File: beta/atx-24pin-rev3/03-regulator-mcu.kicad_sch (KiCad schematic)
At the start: 18 parts, among them SW1 BOOT, SW2 RESET, U1 ESP32-C6-MINI-1-N4, U3 LP5907MFX-3.3

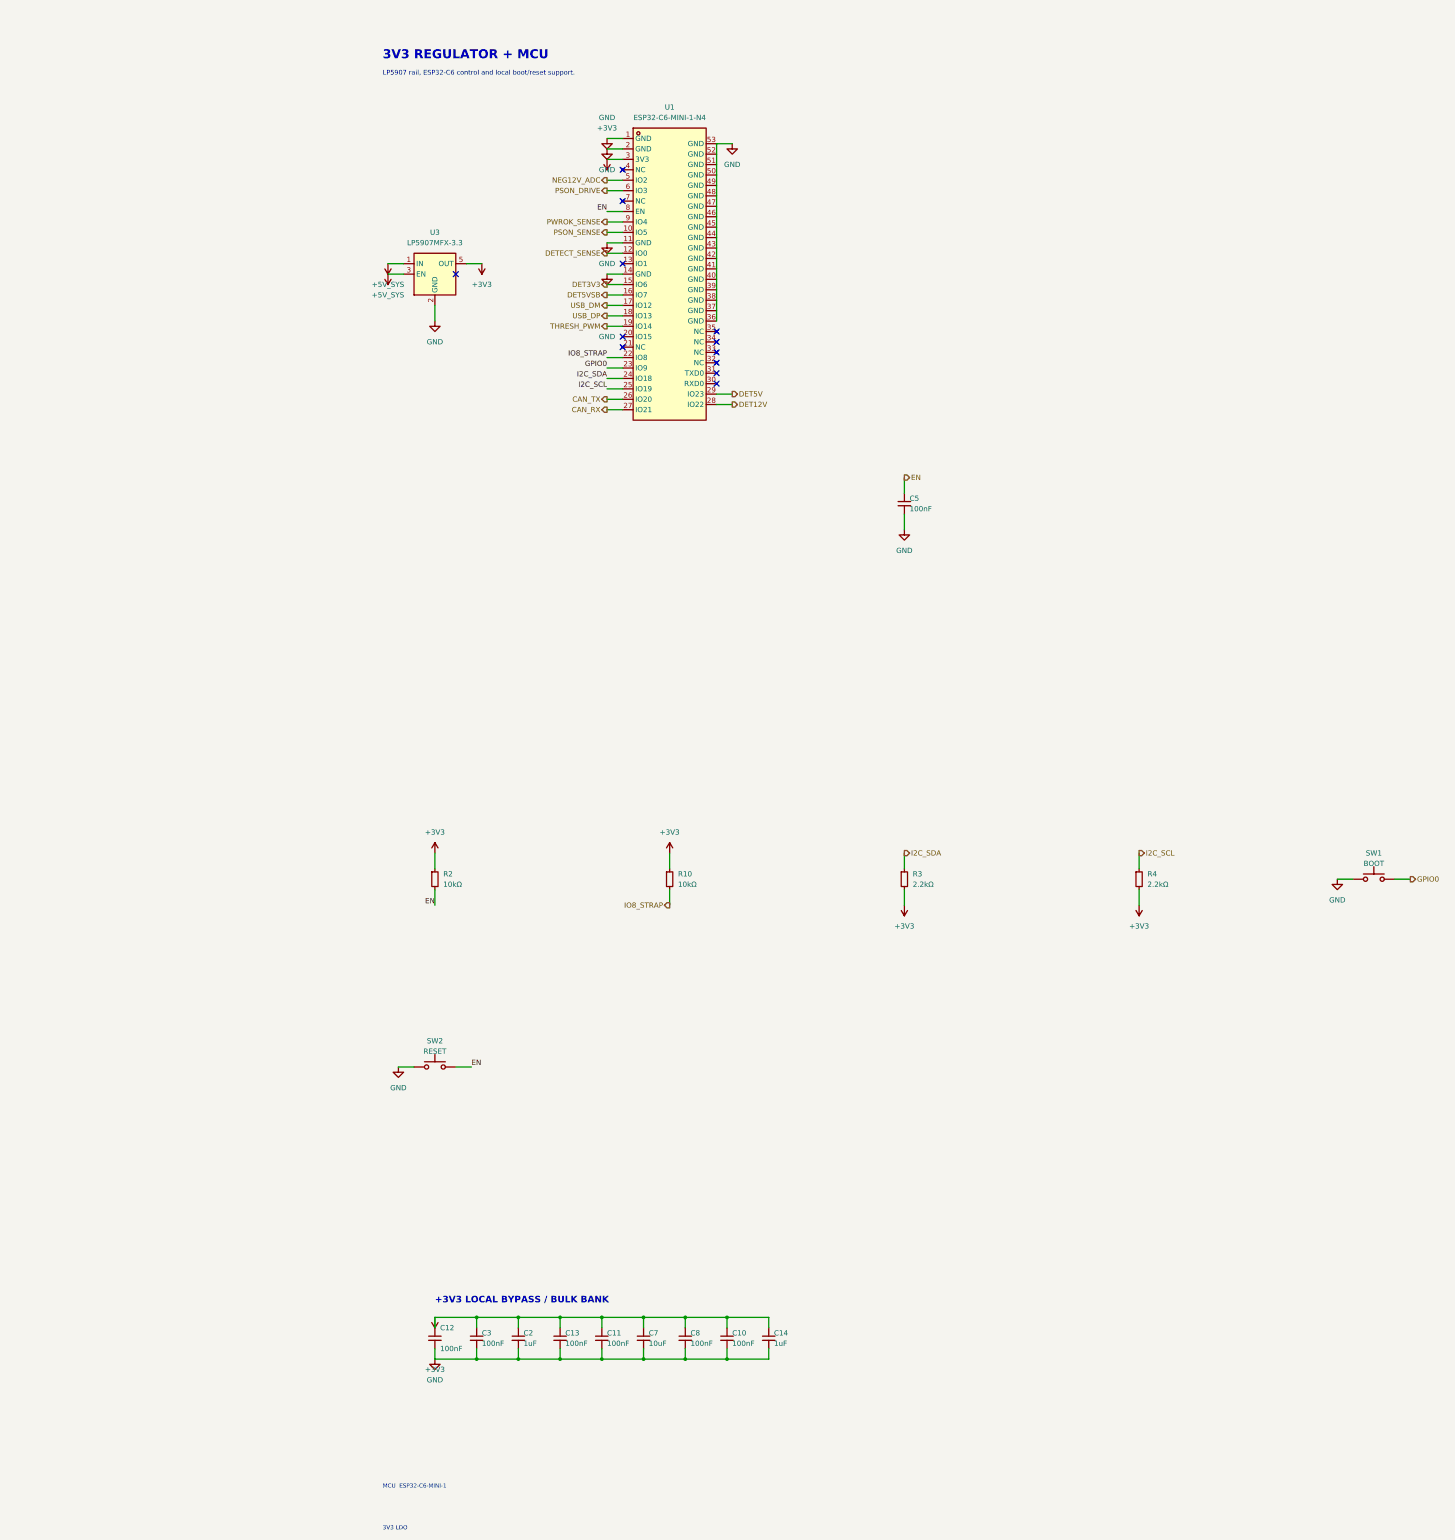
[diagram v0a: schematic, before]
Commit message: Enforce readable BETA schematic layouts
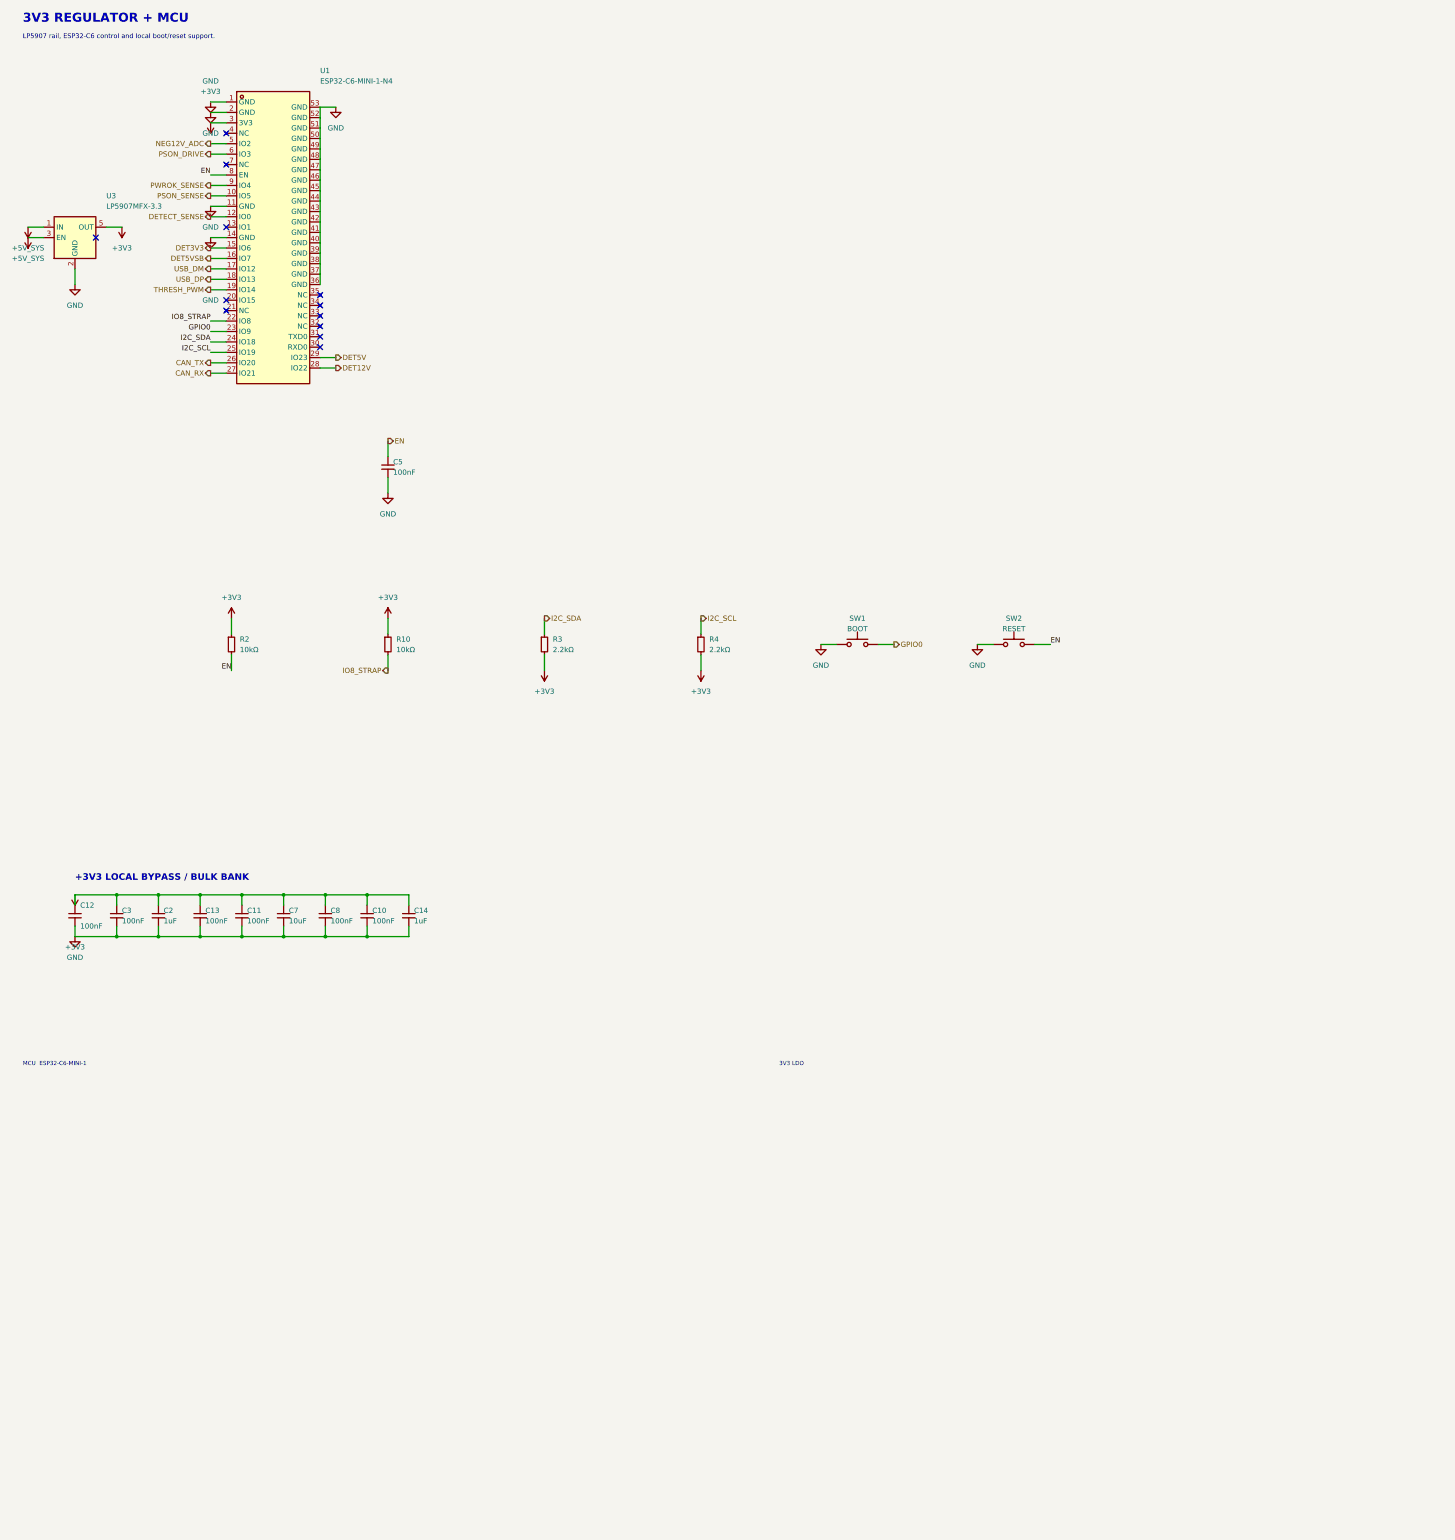
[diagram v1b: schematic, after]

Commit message: Finalize compact Hub and ATX power-layout audit
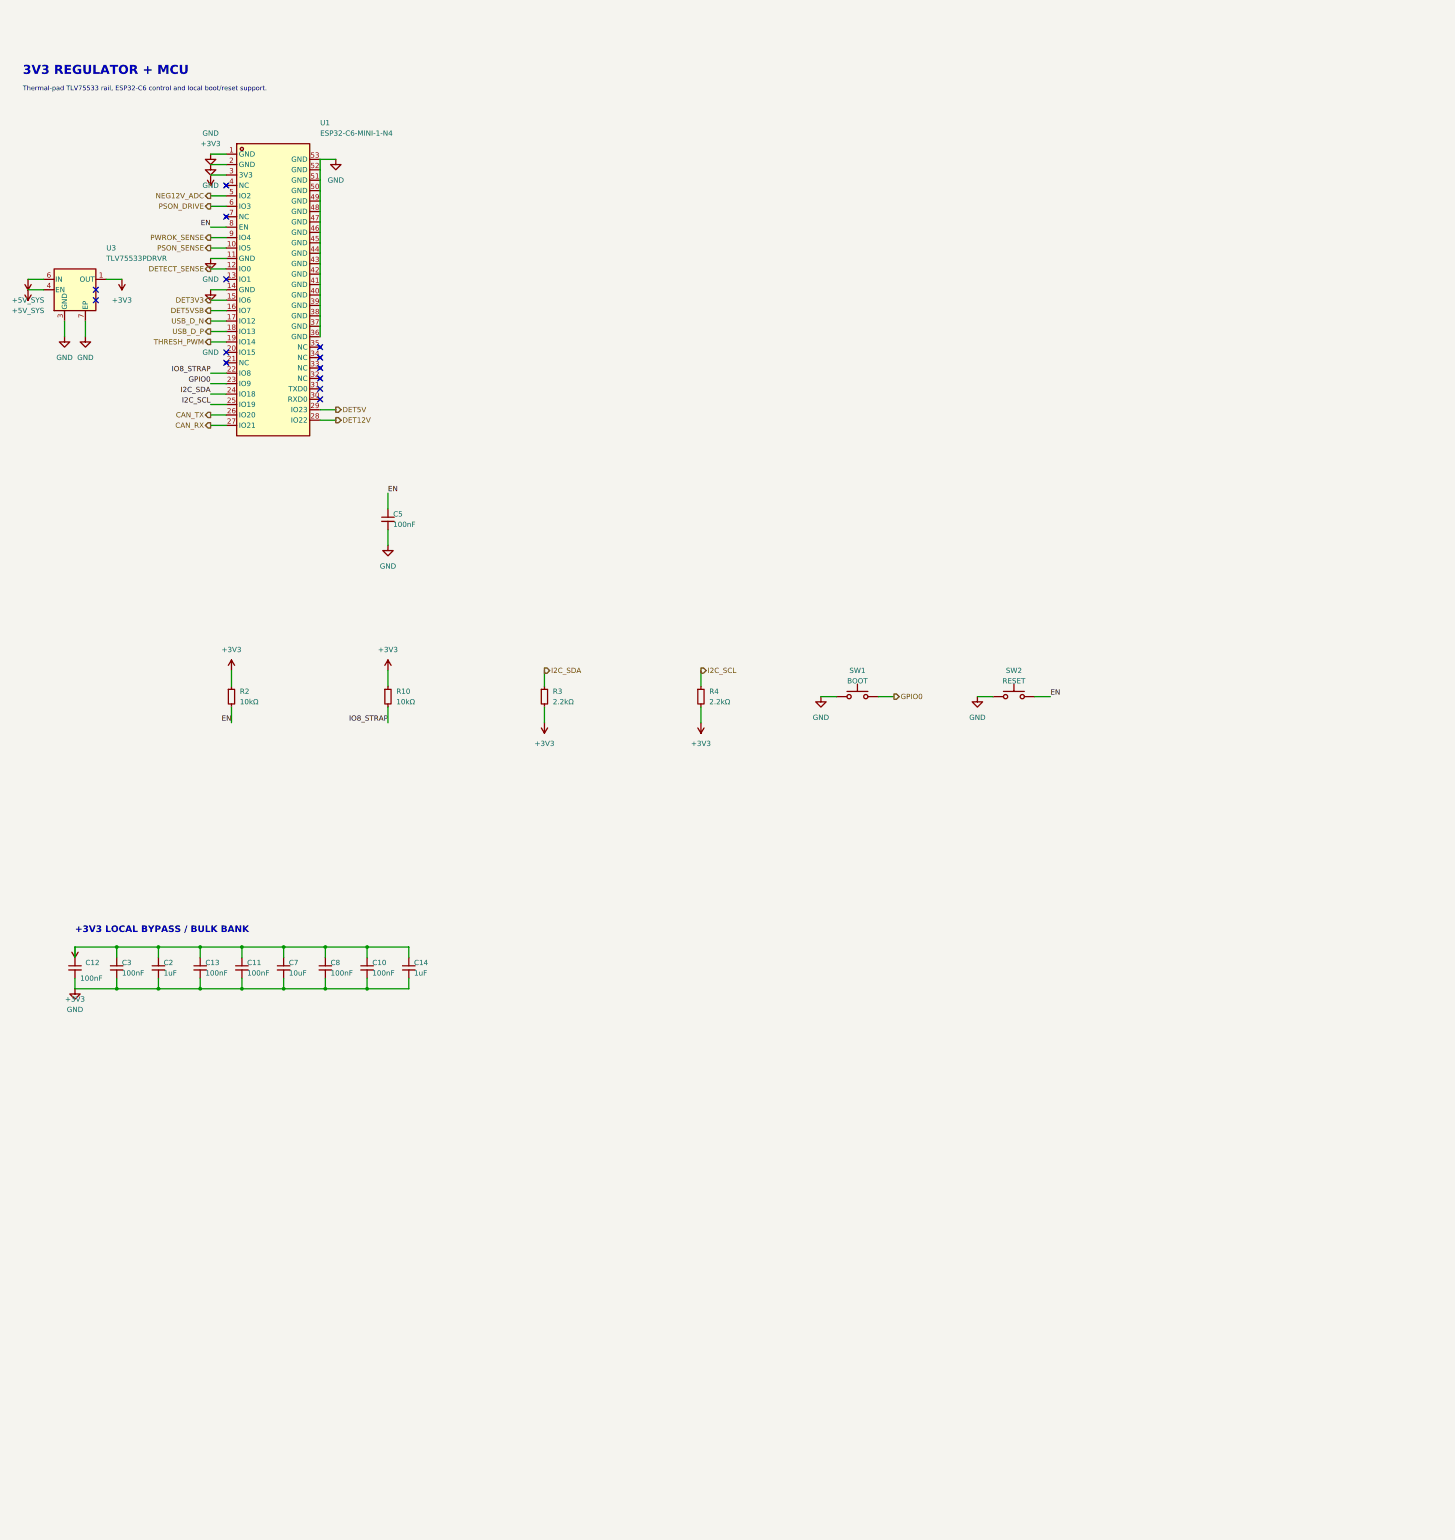
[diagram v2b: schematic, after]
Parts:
- removed U3: LP5907MFX-3.3, cec-Package_TO_SOT_SMD:SOT-23-5, symbol cec-vendor:LP5907MFX-1.2
- added U3: TLV75533PDRVR, cec-Package_SON:WSON-6-1EP_2x2mm_P0.65mm_EP1x1.6mm, symbol cec-vendor:TLV75533PDRVR
- C14: LCSC (none) -> C29936; MPN (none) -> CL10B105KA8NNNC; Manufacturer (none) -> Samsung; Note margin: INA238 U10 VS local bulk (place adjacent) -> TLV75533 output local 1uF X7R; place at U3 OUT/GND.
- C2: LCSC (none) -> C29936; MPN (none) -> CL10B105KA8NNNC; Manufacturer (none) -> Samsung; Note (none) -> Exact 1uF 25V X7R 0603 local bypass capacitor.
- R10, R2: LCSC (none) -> C25744; MPN (none) -> 0402WGF1002TCE; Manufacturer (none) -> UNI-ROYAL
- R3, R4: MPN (none) -> 0402WGF2201TCE; Manufacturer (none) -> UNI-ROYAL
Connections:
- net +3V3: now also U3.1 (OUT)
- net +5V_SYS: now also U3.4 (EN), U3.6 (IN)
- net GND: now also U3.3 (GND), U3.7 (EP)
- net USB_DM renamed USB_D_N
- net USB_DP renamed USB_D_P
- no-connect marks 12 -> 13
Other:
- note added: "Thermal-pad TLV75533 rail, ESP32-C6 control and local boot/reset support."
- note removed: "3V3 LDO"
- note removed: "LP5907 rail, ESP32-C6 control and local boot/reset support."
- note removed: "MCU ESP32-C6-MINI-1"
